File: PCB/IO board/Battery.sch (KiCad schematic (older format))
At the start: 22 parts

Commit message: Schematics Rev 1.0
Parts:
- gave numbers to parts that had none: 21
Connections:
- no-connect marks 0 -> 2

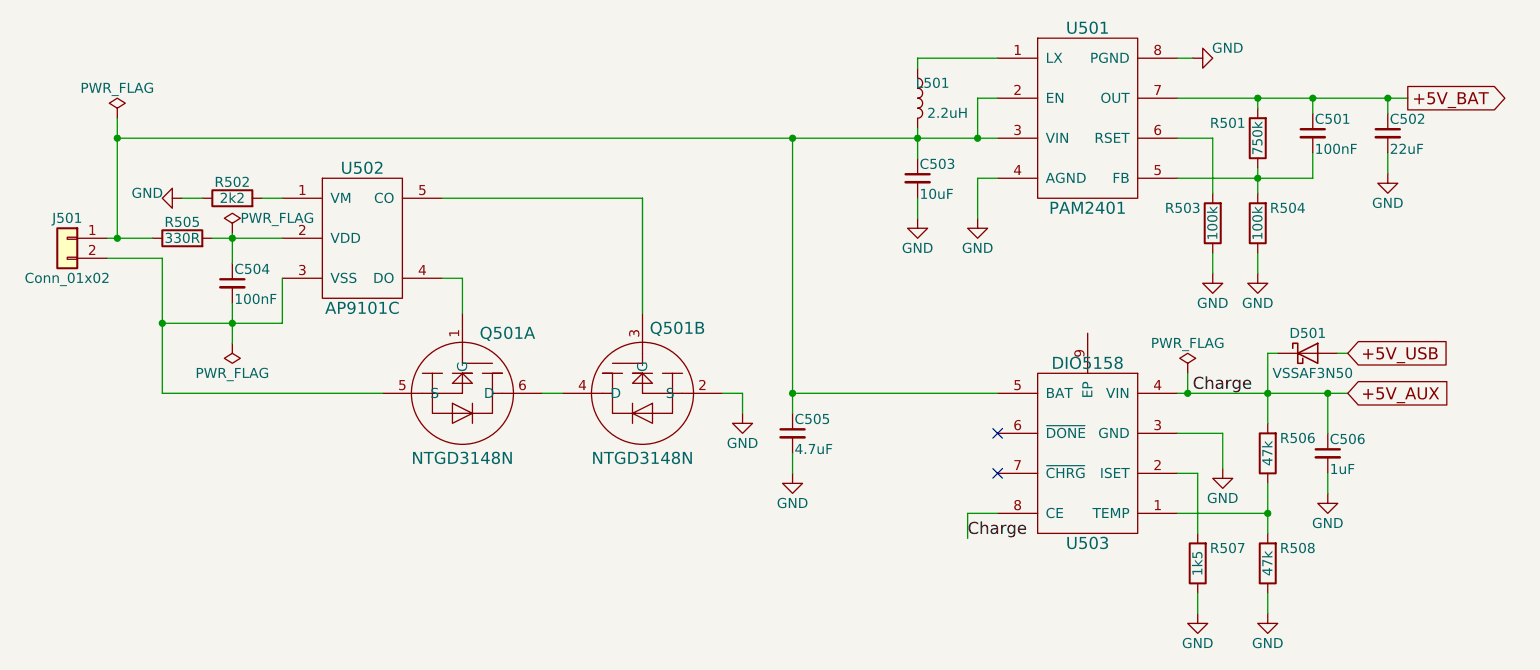
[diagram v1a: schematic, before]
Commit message: Component Placement - No pul-up
ALmost finished component placement expect for pull ups and low pass
filters for switches etc
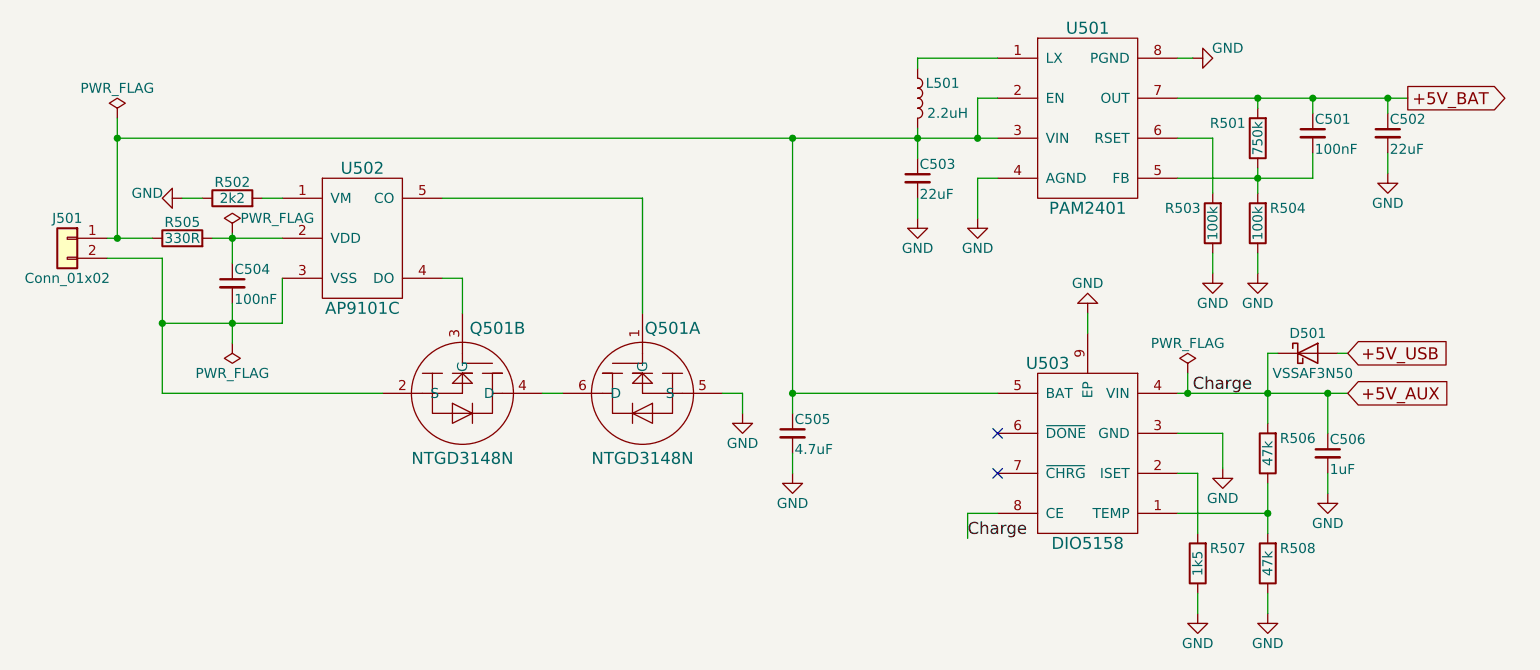
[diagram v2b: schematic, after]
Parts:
- C501, C504, C506: footprint (none) -> Capacitors_SMD:C_0603
- C502, C505: footprint (none) -> Capacitors_SMD:C_0805
- C503: value 10uF -> 22uF; footprint (none) -> Capacitors_SMD:C_0805
- D501: footprint (none) -> Diodes_SMD:D_SMA
- J501: footprint (none) -> ELECTROMECH:Phoenix_1751765
- L501: footprint (none) -> Inductor:L-1008
- Q501: footprint (none) -> Housings_SSOP:TSOP-6_1.65x3.05mm_Pitch0.95mm
- R501, R502, R503, R504, R505, R506, R507, R508: footprint (none) -> Resistors_SMD:R_0603
- U501, U503: footprint (none) -> Housings_SSOP:MSOP-8-1EP_3x3mm_Pitch0.65mm
- U502: footprint (none) -> TO_SOT_Packages_SMD:SOT-23-5
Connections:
- net GND: now also Q501.5 (S), U503.9 (EP); no longer Q501.2 (S)
- net at C504.2, J501.2 (Pin_2), U502.3 (VSS): now also Q501.2 (S); no longer Q501.5 (S)
- net at U502.4 (DO): now also Q501.3 (G); no longer Q501.1 (G)
- net at U502.5 (CO): now also Q501.1 (G); no longer Q501.3 (G)
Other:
- moved on the sheet: Q501A, Q501B
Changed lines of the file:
@@
 F 0 "J501" H 1250 1900 50  0000 C CNN
 F 1 "Conn_01x02" H 1250 1600 50  0000 C CNN
-F 2 "" H 1250 1800 50  0001 C CNN
+F 2 "ELECTROMECH:Phoenix_1751765" H 1250 1800 50  0001 C CNN
 F 3 "" H 1250 1800 50  0001 C CNN
 	1    1250 1800
@@
 F 0 "R505" V 1905 1800 50  0000 C CNN
 F 1 "330R" V 1825 1800 50  0000 C CNN
-F 2 "" V 1755 1800 50  0001 C CNN
+F 2 "Resistors_SMD:R_0603" V 1755 1800 50  0001 C CNN
 F 3 "" H 1825 1800 50  0001 C CNN
 	1    1825 1800
@@
 F 0 "C504" H 2085 2095 50  0000 L CNN
 F 1 "100nF" H 2085 1945 50  0000 L CNN
-F 2 "" H 2075 2025 50  0001 C CNN
+F 2 "Capacitors_SMD:C_0603" H 2075 2025 50  0001 C CNN
 F 3 "" H 2075 2025 50  0001 C CNN
 	1    2075 2025
@@
 F 0 "R502" V 2155 1600 50  0000 C CNN
 F 1 "2k2" V 2075 1600 50  0000 C CNN
-F 2 "" V 2005 1600 50  0001 C CNN
+F 2 "Resistors_SMD:R_0603" V 2005 1600 50  0001 C CNN
 F 3 "" H 2075 1600 50  0001 C CNN
 	1    2075 1600
@@
 F 0 "U502" H 2725 2150 60  0000 C CNN
 F 1 "AP9101C" H 2725 1450 60  0000 C CNN
-F 2 "" H 2525 1800 60  0001 C CNN
+F 2 "TO_SOT_Packages_SMD:SOT-23-5" H 2525 1800 60  0001 C CNN
 F 3 "" H 2525 1800 60  0001 C CNN
 	1    2725 1800
@@
 L NTGD3148N Q501
 U 1 1 5ADF53FA
-P 3225 2575
-F 0 "Q501" V 2925 2800 60  0000 C CNN
-F 1 "NTGD3148N" V 3550 2575 60  0000 C CNN
-F 2 "" H 3225 2575 60  0001 C CNN
-F 3 "" H 3225 2575 60  0001 C CNN
-	1    3225 2575
-	0    1    1    0
+P 4125 2575
+F 0 "Q501" V 3800 2425 60  0000 C CNN
+F 1 "NTGD3148N" V 4450 2575 60  0000 C CNN
+F 2 "Housings_SSOP:TSOP-6_1.65x3.05mm_Pitch0.95mm" H 4125 2575 60  0001 C CNN
+F 3 "" H 4125 2575 60  0001 C CNN
+	1    4125 2575
+	0    -1   1    0
 $EndComp
 $Comp
 L NTGD3148N Q501
 U 2 1 5ADF5479
-P 4125 2575
-F 0 "Q501" V 3800 2400 60  0000 C CNN
-F 1 "NTGD3148N" V 4450 2575 60  0000 C CNN
-F 2 "" H 4125 2575 60  0001 C CNN
-F 3 "" H 4125 2575 60  0001 C CNN
-	2    4125 2575
-	0    -1   1    0
+P 3225 2575
+F 0 "Q501" V 2900 2750 60  0000 C CNN
+F 1 "NTGD3148N" V 3550 2575 60  0000 C CNN
+F 2 "Housings_SSOP:TSOP-6_1.65x3.05mm_Pitch0.95mm" H 3225 2575 60  0001 C CNN
+F 3 "" H 3225 2575 60  0001 C CNN
+	2    3225 2575
+	0    1    1    0
 $EndComp
 $Comp
@@
 F 0 "U501" H 6350 1450 60  0000 C CNN
 F 1 "PAM2401" H 6350 550 60  0000 C CNN
-F 2 "" H 6350 1100 60  0001 C CNN
+F 2 "Housings_SSOP:MSOP-8-1EP_3x3mm_Pitch0.65mm" H 6350 1100 60  0001 C CNN
 F 3 "" H 6350 1100 60  0001 C CNN
 	1    6350 1100
@@
 P 5500 1500
 F 0 "C503" H 5510 1570 50  0000 L CNN
-F 1 "10uF" H 5510 1420 50  0000 L CNN
-F 2 "" H 5500 1500 50  0001 C CNN
+F 1 "22uF" H 5510 1420 50  0000 L CNN
+F 2 "Capacitors_SMD:C_0805" H 5500 1500 50  0001 C CNN
 F 3 "" H 5500 1500 50  0001 C CNN
 	1    5500 1500
@@
 F 0 "R501" H 7350 1225 50  0000 C CNN
 F 1 "750k" V 7200 1300 50  0000 C CNN
-F 2 "" V 7130 1300 50  0001 C CNN
+F 2 "Resistors_SMD:R_0603" V 7130 1300 50  0001 C CNN
 F 3 "" H 7200 1300 50  0001 C CNN
 	1    7200 1300
@@
 F 0 "R504" H 7050 1650 50  0000 C CNN
 F 1 "100k" V 7200 1725 50  0000 C CNN
-F 2 "" V 7130 1725 50  0001 C CNN
+F 2 "Resistors_SMD:R_0603" V 7130 1725 50  0001 C CNN
 F 3 "" H 7200 1725 50  0001 C CNN
 	1    7200 1725
@@
 F 0 "C501" H 7485 1345 50  0000 L CNN
 F 1 "100nF" H 7485 1195 50  0000 L CNN
-F 2 "" H 7475 1275 50  0001 C CNN
+F 2 "Capacitors_SMD:C_0603" H 7475 1275 50  0001 C CNN
 F 3 "" H 7475 1275 50  0001 C CNN
 	1    7475 1275
@@
 F 0 "R503" H 7125 1650 50  0000 C CNN
 F 1 "100k" V 6975 1725 50  0000 C CNN
-F 2 "" V 6905 1725 50  0001 C CNN
+F 2 "Resistors_SMD:R_0603" V 6905 1725 50  0001 C CNN
 F 3 "" H 6975 1725 50  0001 C CNN
 	1    6975 1725
@@
 F 0 "C502" H 7860 1345 50  0000 L CNN
 F 1 "22uF" H 7860 1195 50  0000 L CNN
-F 2 "" H 7850 1275 50  0001 C CNN
+F 2 "Capacitors_SMD:C_0805" H 7850 1275 50  0001 C CNN
 F 3 "" H 7850 1275 50  0001 C CNN
 	1    7850 1275
@@
 U 1 1 5ADF8D43
 P 5500 1100
-F 0 "L501" H 5575 1175 50  0000 C CNN
+F 0 "L501" H 5625 1175 50  0000 C CNN
 F 1 "2.2uH" H 5650 1025 50  0000 C CNN
-F 2 "" H 5500 1100 50  0001 C CNN
+F 2 "Inductor:L-1008" H 5500 1100 50  0001 C CNN
 F 3 "" H 5500 1100 50  0001 C CNN
 	1    5500 1100
@@
 U 1 1 5ADFA0A7
 P 6350 2875
-F 0 "U503" H 6350 3325 60  0000 C CNN
-F 1 "DIO5158" H 6350 2425 60  0000 C CNN
-F 2 "" H 6250 2925 60  0001 C CNN
+F 0 "U503" H 6550 2425 60  0000 C CNN
+F 1 "DIO5158" H 6350 3325 60  0000 C CNN
+F 2 "Housings_SSOP:MSOP-8-1EP_3x3mm_Pitch0.65mm" H 6250 2925 60  0001 C CNN
 F 3 "" H 6250 2925 60  0001 C CNN
 	1    6350 2875
@@
 F 0 "R508" H 7100 3350 50  0000 C CNN
 F 1 "47k" V 7250 3425 50  0000 C CNN
-F 2 "" V 7180 3425 50  0001 C CNN
+F 2 "Resistors_SMD:R_0603" V 7180 3425 50  0001 C CNN
 F 3 "" H 7250 3425 50  0001 C CNN
 	1    7250 3425
@@
 F 0 "R507" H 6750 3350 50  0000 C CNN
 F 1 "1k5" V 6900 3425 50  0000 C CNN
-F 2 "" V 6830 3425 50  0001 C CNN
+F 2 "Resistors_SMD:R_0603" V 6830 3425 50  0001 C CNN
 F 3 "" H 6900 3425 50  0001 C CNN
 	1    6900 3425
@@
 F 0 "R506" H 7100 2800 50  0000 C CNN
 F 1 "47k" V 7250 2875 50  0000 C CNN
-F 2 "" V 7180 2875 50  0001 C CNN
+F 2 "Resistors_SMD:R_0603" V 7180 2875 50  0001 C CNN
 F 3 "" H 7250 2875 50  0001 C CNN
 	1    7250 2875
@@
 F 0 "C506" H 7560 2945 50  0000 L CNN
 F 1 "1uF" H 7560 2795 50  0000 L CNN
-F 2 "" H 7550 2875 50  0001 C CNN
+F 2 "Capacitors_SMD:C_0603" H 7550 2875 50  0001 C CNN
 F 3 "" H 7550 2875 50  0001 C CNN
 	1    7550 2875
@@
 F 0 "D501" H 7450 2475 50  0000 C CNN
 F 1 "VSSAF3N50" H 7475 2275 50  0000 C CNN
-F 2 "" H 7450 2375 50  0001 C CNN
+F 2 "Diodes_SMD:D_SMA" H 7450 2375 50  0001 C CNN
 F 3 "" H 7450 2375 50  0001 C CNN
 	1    7450 2375
@@
 F 0 "C505" H 4885 2845 50  0000 L CNN
 F 1 "4.7uF" H 4885 2695 50  0000 L CNN
-F 2 "" H 4875 2775 50  0001 C CNN
+F 2 "Capacitors_SMD:C_0805" H 4875 2775 50  0001 C CNN
 F 3 "" H 4875 2775 50  0001 C CNN
 	1    4875 2775
@@
 Connection ~ 6850 2575
 Connection ~ 1500 1300
+$Comp
+L GND #PWR068
+U 1 1 5AEAA2CE
+P 6350 2175
+F 0 "#PWR068" H 6350 1925 50  0001 C CNN
+F 1 "GND" H 6350 2025 50  0000 C CNN
+F 2 "" H 6350 2175 50  0001 C CNN
+F 3 "" H 6350 2175 50  0001 C CNN
+	1    6350 2175
+	-1   0    0    1
+$EndComp
+Wire Wire Line
+	6350 2175 6350 2275
 $EndSCHEMATC

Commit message: PCB Backup
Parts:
- U501: footprint Housings_SSOP:MSOP-8-1EP_3x3mm_Pitch0.65mm -> Housings_SSOP:MSOP-8_3x3mm_Pitch0.65mm
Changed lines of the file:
@@
 F 0 "U501" H 6350 1450 60  0000 C CNN
 F 1 "PAM2401" H 6350 550 60  0000 C CNN
-F 2 "Housings_SSOP:MSOP-8-1EP_3x3mm_Pitch0.65mm" H 6350 1100 60  0001 C CNN
+F 2 "Housings_SSOP:MSOP-8_3x3mm_Pitch0.65mm" H 6350 1100 60  0001 C CNN
 F 3 "" H 6350 1100 60  0001 C CNN
 	1    6350 1100
